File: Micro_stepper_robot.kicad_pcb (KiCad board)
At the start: 2 copper layers, 37 x 47 mm, 8 parts, among them J1 Conn_01x04_Male, J2 Conn_01x04_Male, J3 Conn_01x04_Male, J4 Conn_01x04_Male, M1 Stepper_Motor_bipolar, M2 Stepper_Motor_bipolar, M3 Stepper_Motor_bipolar, M4 Stepper_Motor_bipolar

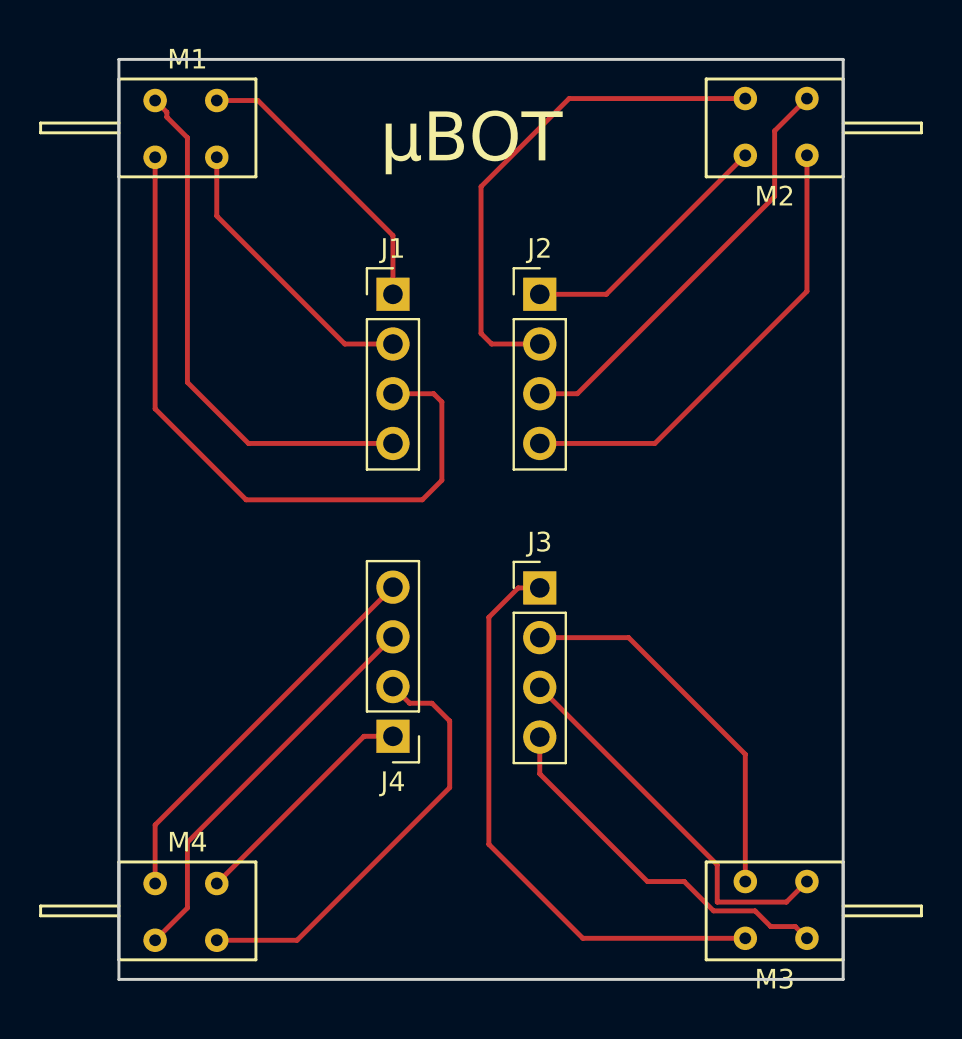
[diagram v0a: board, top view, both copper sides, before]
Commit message: cleaned up silk screen
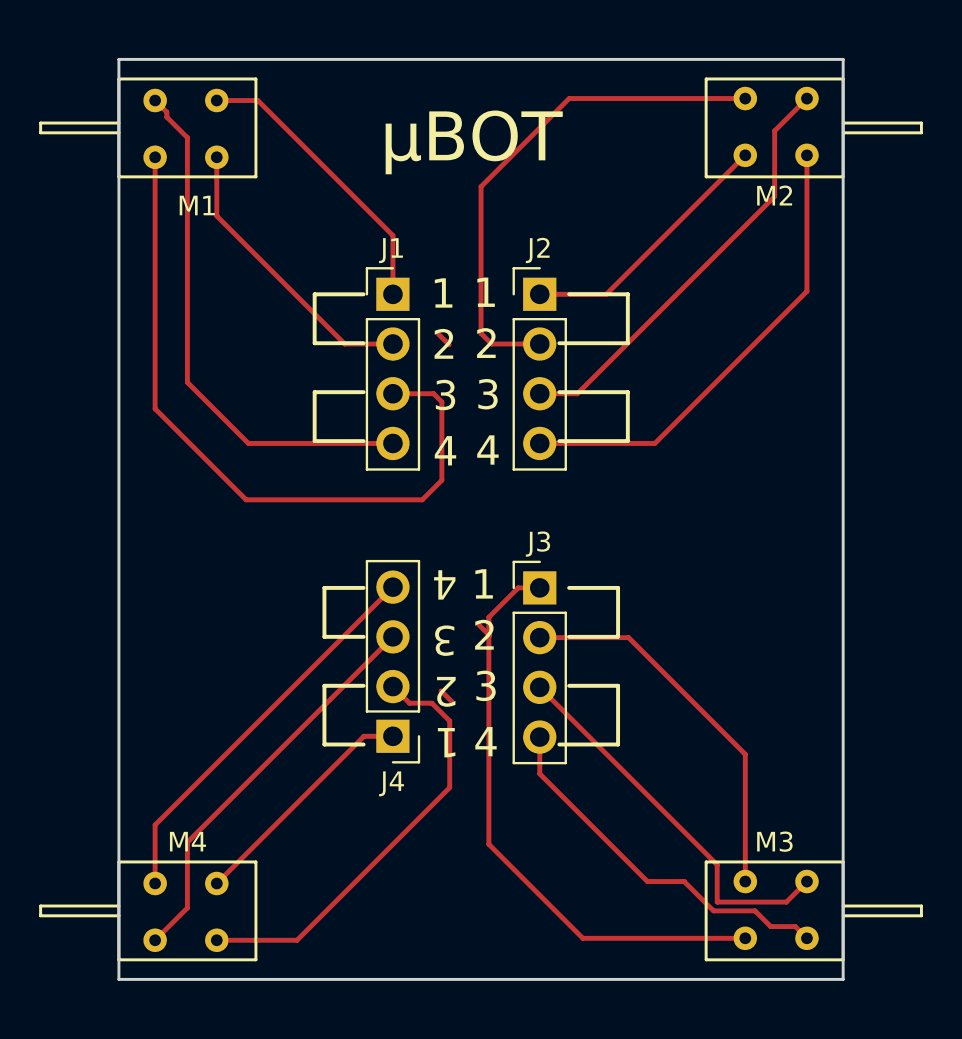
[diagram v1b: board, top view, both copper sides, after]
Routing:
- net Net-(J3-Pad1): track 29.9 -> 31.4 mm
- net Net-(J2-Pad2): track 26.1 -> 26.9 mm
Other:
- board text added: "1"
- board text added: "2"
- board text added: "3"
- board text added: "4"
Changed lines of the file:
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@@
   (general
     (thickness 1.6)
-    (drawings 5)
-    (tracks 66)
+    (drawings 45)
+    (tracks 69)
     (zones 0)
     (modules 8)
@@
   (module my_footprints:micro_stepper1 (layer F.Cu)
     (at 107.5 71.5 180)
-    (fp_text reference M1 (at 0 3.5 180) (layer F.SilkS)
+    (fp_text reference M1 (at -0.5 -4 180) (layer F.SilkS)
       (effects (font (size 1 1) (thickness 0.15)))
     )
@@
   (module my_footprints:micro_stepper1 (layer F.Cu)
     (at 137.5 111.5)
-    (fp_text reference M3 (at 0 3.5) (layer F.SilkS)
+    (fp_text reference M3 (at 0 -3.5) (layer F.SilkS)
       (effects (font (size 1 1) (thickness 0.15)))
     )
@@
       (rotate (xyz 0 0 0))
     )
+  )
+  (gr_line (start 114.5 103) (end 116.5 103) (layer F.SilkS) (width 0.2))
+  (gr_line (start 114.5 100) (end 114.5 103) (layer F.SilkS) (width 0.2))
+  (gr_line (start 116.5 100) (end 114.5 100) (layer F.SilkS) (width 0.2))
+  (gr_line (start 114.5 97.5) (end 116.5 97.5) (layer F.SilkS) (width 0.2))
+  (gr_line (start 114.5 95) (end 114.5 97.5) (layer F.SilkS) (width 0.2))
+  (gr_line (start 116.5 95) (end 114.5 95) (layer F.SilkS) (width 0.2))
+  (gr_line (start 129.5 103) (end 126.5 103) (layer F.SilkS) (width 0.2))
+  (gr_line (start 129.5 100) (end 129.5 103) (layer F.SilkS) (width 0.2))
+  (gr_line (start 127 100) (end 129.5 100) (layer F.SilkS) (width 0.2))
+  (gr_line (start 129.5 97.5) (end 127 97.5) (layer F.SilkS) (width 0.2))
+  (gr_line (start 129.5 95) (end 129.5 97.5) (layer F.SilkS) (width 0.2))
+  (gr_line (start 127 95) (end 129.5 95) (layer F.SilkS) (width 0.2))
+  (gr_line (start 114 87.5) (end 116.5 87.5) (layer F.SilkS) (width 0.2))
+  (gr_line (start 114 85) (end 114 87.5) (layer F.SilkS) (width 0.2))
+  (gr_line (start 116.5 85) (end 114 85) (layer F.SilkS) (width 0.2))
+  (gr_line (start 114 82.5) (end 116.5 82.5) (layer F.SilkS) (width 0.2))
+  (gr_line (start 114 80) (end 114 82.5) (layer F.SilkS) (width 0.2))
+  (gr_line (start 116.5 80) (end 114 80) (layer F.SilkS) (width 0.2))
+  (gr_line (start 130 87.5) (end 126.5 87.5) (layer F.SilkS) (width 0.2))
+  (gr_line (start 130 85) (end 130 87.5) (layer F.SilkS) (width 0.2))
+  (gr_line (start 126.5 85) (end 130 85) (layer F.SilkS) (width 0.2))
+  (gr_line (start 130 82.5) (end 126.5 82.5) (layer F.SilkS) (width 0.2))
+  (gr_line (start 130 80) (end 130 82.5) (layer F.SilkS) (width 0.2))
+  (gr_line (start 127 80) (end 130 80) (layer F.SilkS) (width 0.2))
+  (gr_text 4 (at 120.64 94.79 180) (layer F.SilkS)
+    (effects (font (size 1.5 1.5) (thickness 0.3)))
+  )
+  (gr_text 3 (at 120.64 97.64 180) (layer F.SilkS)
+    (effects (font (size 1.5 1.5) (thickness 0.3)))
+  )
+  (gr_text 2 (at 120.7 100.24 180) (layer F.SilkS)
+    (effects (font (size 1.5 1.5) (thickness 0.3)))
+  )
+  (gr_text 1 (at 120.76 102.85 180) (layer F.SilkS)
+    (effects (font (size 1.5 1.5) (thickness 0.3)))
+  )
+  (gr_text 2 (at 122.7 97.46) (layer F.SilkS)
+    (effects (font (size 1.5 1.5) (thickness 0.3)))
+  )
+  (gr_text 1 (at 122.64 94.85) (layer F.SilkS)
+    (effects (font (size 1.5 1.5) (thickness 0.3)))
+  )
+  (gr_text 4 (at 122.76 102.91) (layer F.SilkS)
+    (effects (font (size 1.5 1.5) (thickness 0.3)))
+  )
+  (gr_text 3 (at 122.76 100.06) (layer F.SilkS)
+    (effects (font (size 1.5 1.5) (thickness 0.3)))
+  )
+  (gr_text 2 (at 120.63 82.6) (layer F.SilkS)
+    (effects (font (size 1.5 1.5) (thickness 0.3)))
+  )
+  (gr_text 1 (at 120.57 79.99) (layer F.SilkS)
+    (effects (font (size 1.5 1.5) (thickness 0.3)))
+  )
+  (gr_text 4 (at 120.69 88.05) (layer F.SilkS)
+    (effects (font (size 1.5 1.5) (thickness 0.3)))
+  )
+  (gr_text 3 (at 120.69 85.2) (layer F.SilkS)
+    (effects (font (size 1.5 1.5) (thickness 0.3)))
+  )
+  (gr_text 4 (at 122.86 88.01) (layer F.SilkS)
+    (effects (font (size 1.5 1.5) (thickness 0.3)))
+  )
+  (gr_text 3 (at 122.86 85.16) (layer F.SilkS)
+    (effects (font (size 1.5 1.5) (thickness 0.3)))
+  )
+  (gr_text 2 (at 122.8 82.56) (layer F.SilkS)
+    (effects (font (size 1.5 1.5) (thickness 0.3)))
+  )
+  (gr_text 1 (at 122.74 79.95) (layer F.SilkS)
+    (effects (font (size 1.5 1.5) (thickness 0.3)))
   )
   (gr_text μBOT (at 122 72) (layer F.SilkS)
@@
   (segment (start 122.5 74.5) (end 127 70) (width 0.25) (layer F.Cu) (net 6))
   (segment (start 127 70) (end 136 70) (width 0.25) (layer F.Cu) (net 6))
+  (segment (start 120.87 82.58) (end 120.33 82.04) (width 0.25) (layer F.Cu) (net 6))
+  (segment (start 122.94 97.44) (end 122.4 96.9) (width 0.25) (layer F.Cu) (net 12))
   (segment (start 125.5 85.08) (end 127.42 85.08) (width 0.25) (layer F.Cu) (net 7))
   (segment (start 127.42 85.08) (end 137.5 75) (width 0.25) (layer F.Cu) (net 7))
@@
   (segment (start 122.9 108.1) (end 127.7 112.9) (width 0.25) (layer F.Cu) (net 12))
   (segment (start 124.4 95) (end 122.9 96.5) (width 0.25) (layer F.Cu) (net 12))
+  (segment (start 120.46 100.26) (end 121 100.8) (width 0.25) (layer F.Cu) (net 12))
   (segment (start 105.85 107.11) (end 105.85 110.1) (width 0.25) (layer F.Cu) (net 13))
   (segment (start 118 94.96) (end 105.85 107.11) (width 0.25) (layer F.Cu) (net 13))

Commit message: updated silkscreen to v2
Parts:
- M1, M2, M3, M4: footprint my_footprints:micro_stepper1 -> kicad_footprints:micro_stepper1
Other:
- board text added: "μBOT v2"
- board text removed: "μBOT"
